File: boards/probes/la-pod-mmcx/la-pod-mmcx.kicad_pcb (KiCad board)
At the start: 4 copper layers, 80 x 20.8 mm, 16 parts, among them J1 MMCX-J-P-H-ST-EM1, J2 MMCX-J-P-H-ST-EM1, J3 MMCX-J-P-H-ST-EM1, J4 MMCX-J-P-H-ST-EM1, J5 LSHM-120-02.5-L-DV-A-N-K-TR, J6 MMCX-J-P-H-ST-EM1, J7 MMCX-J-P-H-ST-EM1, J8 MMCX-J-P-H-ST-EM1, J9 MMCX-J-P-H-ST-EM1, U1 24Cxx-DFN8

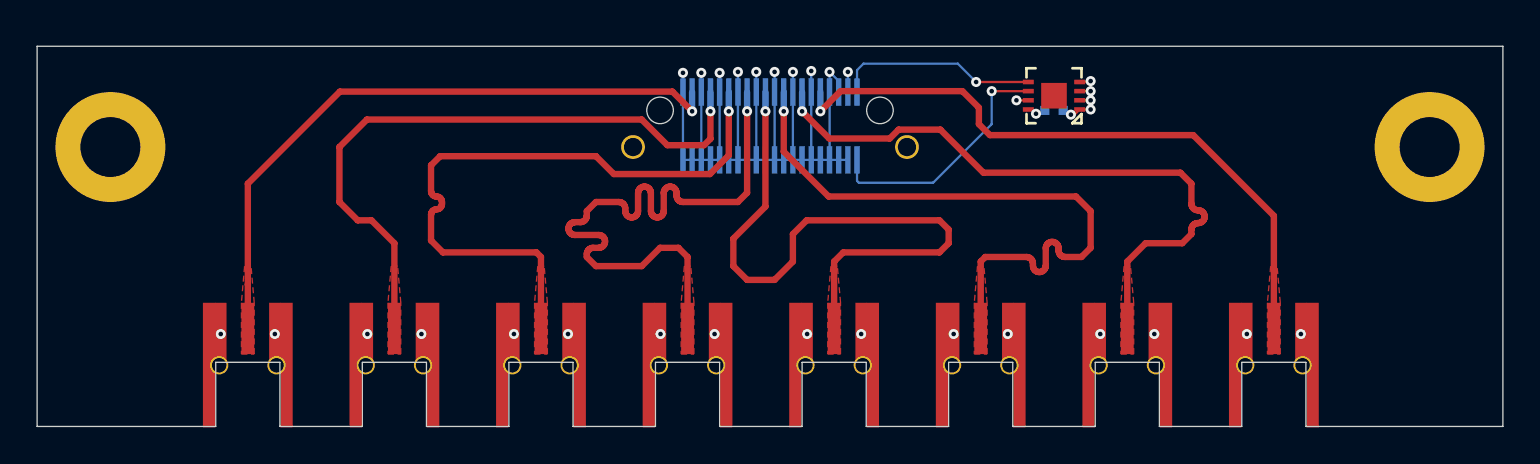
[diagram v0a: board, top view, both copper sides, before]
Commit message: Final version of la-pod-mmcx after layout review
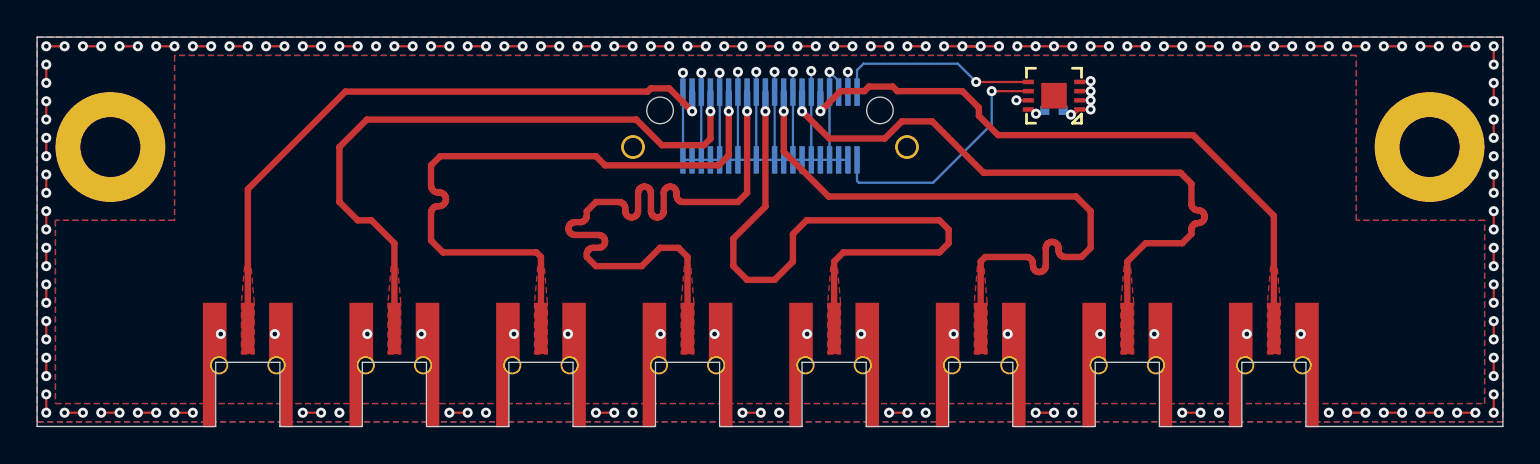
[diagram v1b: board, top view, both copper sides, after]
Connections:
- MH1 pad 1: (no net) -> /GND
- MH2 pad 1: (no net) -> /GND
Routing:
- net /GND: track 193.9 -> 393.0 mm, vias 30 -> 188
- added copper zone on B.Cu, net /GND
- added copper zone on F.Cu, net /GND
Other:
- board size 80 x 20.8 mm -> 80 x 21.2 mm
- board text added: "MEAD MMCX Input Bridge A. Zonenberg / v0.1 / 2020-06-03"
- board text removed: "MEAD MMCX Input Bridge A. Zonenberg / v0.1 / 2020-06-02"

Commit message: Tweaks to la-pod-mmcx mounting hole placement
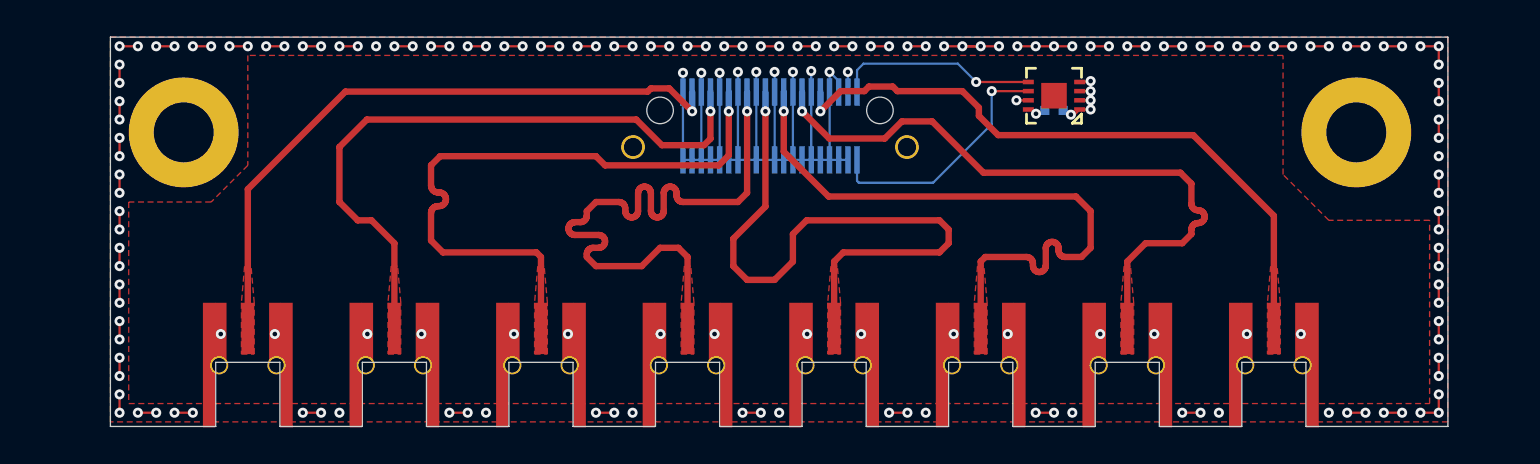
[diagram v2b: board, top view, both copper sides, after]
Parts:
- moved G*** 50.6 mm to (124.6, 56.9)
- moved MH1 4.08 mm to (70.5, 57.7)
- moved MH2 4.08 mm to (134.5, 57.7)
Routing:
- net /GND: track 393.0 -> 371.6 mm, vias 188 -> 174
- removed copper zone on B.Cu, net /GND
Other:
- board size 80 x 21.2 mm -> 73 x 21.2 mm

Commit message: la-pod-mmcx: fixed ground pours colliding with impedance matching cutouts, fixed missing soldermask cutouts on bottom side of board shield ring
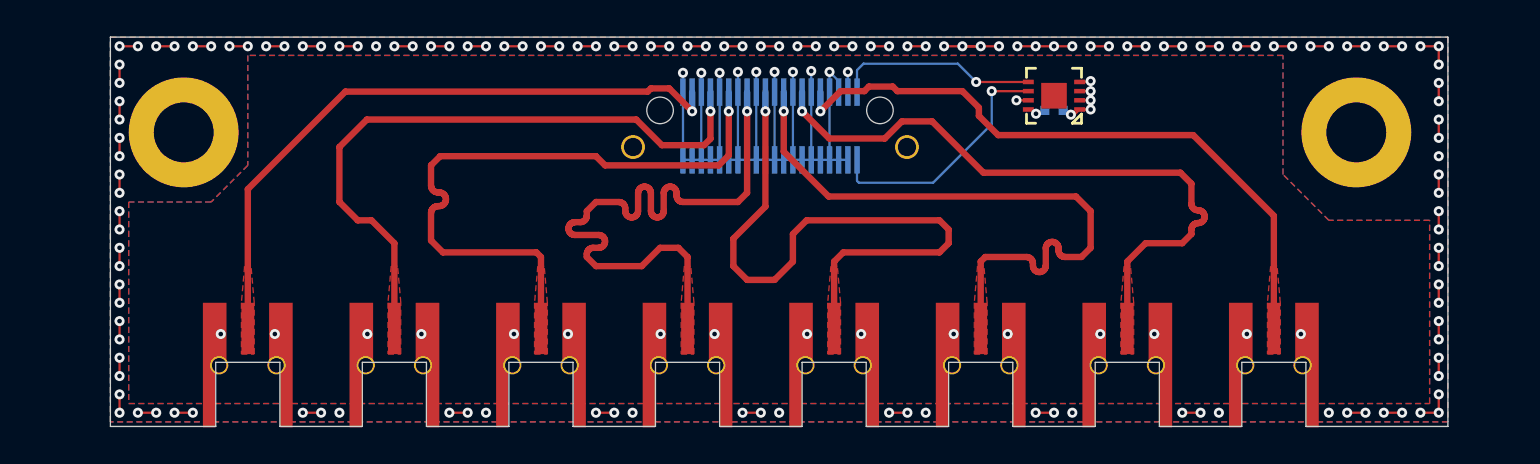
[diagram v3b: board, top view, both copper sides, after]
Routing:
- net /GND: track 371.6 -> 439.5 mm
- added copper zone on B.Cu, net /GND
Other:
- board text added: "MEAD MMCX Input Bridge A. Zonenberg / v0.1 / 2020-06-04"
- board text removed: "MEAD MMCX Input Bridge A. Zonenberg / v0.1 / 2020-06-03"
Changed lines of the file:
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@@
     (thickness 1.6)
     (drawings 37)
-    (tracks 801)
+    (tracks 822)
     (zones 0)
     (modules 16)
@@
     )
   )
-  (gr_text "MEAD MMCX Input Bridge\nA. Zonenberg / v0.1 / 2020-06-03" (at 82 63) (layer B.SilkS)
+  (gr_text "MEAD MMCX Input Bridge\nA. Zonenberg / v0.1 / 2020-06-04" (at 82 63) (layer B.SilkS)
     (effects (font (size 0.75 0.75) (thickness 0.1)) (justify mirror))
   )
@@
   (segment (start 123.475 68.705) (end 123.475 65.775) (width 0.125) (layer In1.Cu) (net 1))
   (segment (start 128.5 65.75) (end 123.5 65.75) (width 0.125) (layer In1.Cu) (net 1))
-  (segment (start 123.5 65.75) (end 120.75 65.75) (width 0.125) (layer In1.Cu) (net 1))
   (via (at 115.475 68.705) (size 0.55) (drill 0.25) (layers F.Cu B.Cu) (net 1))
   (via (at 112.525 68.705) (size 0.55) (drill 0.25) (layers F.Cu B.Cu) (net 1))
@@
   (segment (start 115.475 65.775) (end 115.5 65.75) (width 0.125) (layer In1.Cu) (net 1))
   (segment (start 115.475 68.705) (end 115.475 65.775) (width 0.125) (layer In1.Cu) (net 1))
-  (segment (start 115.5 65.75) (end 112.5 65.75) (width 0.125) (layer In1.Cu) (net 1))
   (via (at 107.475 68.705) (size 0.55) (drill 0.25) (layers F.Cu B.Cu) (net 1))
   (segment (start 107.475 65.775) (end 107.5 65.75) (width 0.125) (layer In1.Cu) (net 1))
-  (segment (start 112.5 65.75) (end 107.5 65.75) (width 0.125) (layer In1.Cu) (net 1))
   (segment (start 107.475 68.705) (end 107.475 65.775) (width 0.125) (layer In1.Cu) (net 1))
   (via (at 104.525 68.705) (size 0.55) (drill 0.25) (layers F.Cu B.Cu) (net 1))
   (segment (start 104.525 65.775) (end 104.5 65.75) (width 0.125) (layer In1.Cu) (net 1))
   (segment (start 104.525 68.705) (end 104.525 65.775) (width 0.125) (layer In1.Cu) (net 1))
-  (segment (start 107.5 65.75) (end 104.5 65.75) (width 0.125) (layer In1.Cu) (net 1))
   (via (at 99.475 68.705) (size 0.55) (drill 0.25) (layers F.Cu B.Cu) (net 1))
   (via (at 96.525 68.705) (size 0.55) (drill 0.25) (layers F.Cu B.Cu) (net 1))
@@
   (segment (start 104.5 65.75) (end 99.5 65.75) (width 0.125) (layer In1.Cu) (net 1))
   (segment (start 99.475 68.705) (end 99.475 65.775) (width 0.125) (layer In1.Cu) (net 1))
-  (segment (start 99.5 65.75) (end 96.5 65.75) (width 0.125) (layer In1.Cu) (net 1))
   (via (at 88.525 68.705) (size 0.55) (drill 0.25) (layers F.Cu B.Cu) (net 1))
   (via (at 91.475 68.705) (size 0.55) (drill 0.25) (layers F.Cu B.Cu) (net 1))
   (segment (start 91.475 65.775) (end 91.5 65.75) (width 0.125) (layer In1.Cu) (net 1))
   (segment (start 91.475 68.705) (end 91.475 65.775) (width 0.125) (layer In1.Cu) (net 1))
-  (segment (start 96.5 65.75) (end 91.5 65.75) (width 0.125) (layer In1.Cu) (net 1))
   (segment (start 88.5 67.2875) (end 88.5 65.75) (width 0.125) (layer In1.Cu) (net 1))
   (segment (start 88.525 67.3125) (end 88.5 67.2875) (width 0.125) (layer In1.Cu) (net 1))
   (segment (start 88.525 68.705) (end 88.525 67.3125) (width 0.125) (layer In1.Cu) (net 1))
-  (segment (start 91.5 65.75) (end 88.5 65.75) (width 0.125) (layer In1.Cu) (net 1))
   (via (at 83.475 68.705) (size 0.55) (drill 0.25) (layers F.Cu B.Cu) (net 1))
   (via (at 80.525 68.705) (size 0.55) (drill 0.25) (layers F.Cu B.Cu) (net 1))
@@
   (segment (start 83.475 68.705) (end 83.475 66.875) (width 0.125) (layer In1.Cu) (net 1))
   (segment (start 83.5 66.85) (end 83.5 65.75) (width 0.125) (layer In1.Cu) (net 1))
-  (segment (start 88.5 65.75) (end 83.5 65.75) (width 0.125) (layer In1.Cu) (net 1))
-  (segment (start 83.5 65.75) (end 80.5 65.75) (width 0.125) (layer In1.Cu) (net 1))
-  (via (at 75.475 68.705) (size 0.55) (drill 0.25) (layers F.Cu B.Cu) (net 1))
   (segment (start 75.475 68.705) (end 75.475 65.775) (width 0.125) (layer In1.Cu) (net 1))
   (segment (start 75.475 65.775) (end 75.5 65.75) (width 0.125) (layer In1.Cu) (net 1))
   (segment (start 80.5 65.75) (end 75.5 65.75) (width 0.125) (layer In1.Cu) (net 1))
-  (segment (start 131.475 66.875) (end 131.475 68.705) (width 0.125) (layer In1.Cu) (net 1))
-  (segment (start 130.35 65.75) (end 131.475 66.875) (width 0.125) (layer In1.Cu) (net 1))
-  (segment (start 128.5 65.75) (end 130.35 65.75) (width 0.125) (layer In1.Cu) (net 1))
   (segment (start 97.75 56.375) (end 97.75 59.2) (width 0.125) (layer B.Cu) (net 1))
   (segment (start 97.75 55.5) (end 97.75 56.375) (width 0.125) (layer B.Cu) (net 1))
@@
   (segment (start 99.75 65.5) (end 99.475 65.775) (width 0.125) (layer In1.Cu) (net 1))
   (segment (start 99.75 54.45) (end 99.75 65.5) (width 0.125) (layer In1.Cu) (net 1))
-  (via (at 72.525 68.705) (size 0.55) (drill 0.25) (layers F.Cu B.Cu) (net 1))
-  (segment (start 75.475 68.705) (end 72.525 68.705) (width 0.125) (layer In1.Cu) (net 1))
   (via (at 71 73) (size 0.55) (drill 0.25) (layers F.Cu B.Cu) (net 1))
   (segment (start 71 69.7925) (end 71 73) (width 0.125) (layer In1.Cu) (net 1))
@@
   (segment (start 139 54) (end 139 53) (width 0.125) (layer F.Cu) (net 1))
   (segment (start 139 72) (end 139 73) (width 0.125) (layer F.Cu) (net 1))
+  (segment (start 72.525 68.705) (end 72.525 63.175) (width 0.125) (layer In1.Cu) (net 1))
+  (segment (start 72.525 63.175) (end 73.25 62.45) (width 0.125) (layer In1.Cu) (net 1))
+  (segment (start 75.5 63.5) (end 75.5 65.75) (width 0.125) (layer In1.Cu) (net 1))
+  (segment (start 74.45 62.45) (end 75.5 63.5) (width 0.125) (layer In1.Cu) (net 1))
+  (via (at 72.525 68.705) (size 0.55) (drill 0.25) (layers F.Cu B.Cu) (net 1))
+  (via (at 75.475 68.705) (size 0.55) (drill 0.25) (layers F.Cu B.Cu) (net 1))
+  (segment (start 74.35 62.45) (end 74.45 62.45) (width 0.125) (layer In1.Cu) (net 1))
+  (segment (start 73.25 62.45) (end 74.35 62.45) (width 0.125) (layer In1.Cu) (net 1))
+  (segment (start 129.6 62.45) (end 131.475 64.325) (width 0.125) (layer In1.Cu) (net 1))
+  (segment (start 131.475 64.325) (end 131.475 67.125) (width 0.125) (layer In1.Cu) (net 1))
+  (segment (start 131.475 67.125) (end 131.475 68.705) (width 0.125) (layer In1.Cu) (net 1))
+  (segment (start 128.5 62.65) (end 128.3 62.45) (width 0.125) (layer In1.Cu) (net 1))
+  (segment (start 128.5 65.75) (end 128.5 62.65) (width 0.125) (layer In1.Cu) (net 1))
+  (segment (start 128.3 62.45) (end 129.6 62.45) (width 0.125) (layer In1.Cu) (net 1))
+  (segment (start 123.475 65.775) (end 123.475 62.475) (width 0.125) (layer In1.Cu) (net 1))
+  (segment (start 123.475 62.475) (end 123.45 62.45) (width 0.125) (layer In1.Cu) (net 1))
+  (segment (start 123.45 62.45) (end 128.3 62.45) (width 0.125) (layer In1.Cu) (net 1))
+  (segment (start 115.5 62.55) (end 115.6 62.45) (width 0.125) (layer In1.Cu) (net 1))
+  (segment (start 115.5 65.75) (end 115.5 62.55) (width 0.125) (layer In1.Cu) (net 1))
+  (segment (start 115.6 62.45) (end 123.45 62.45) (width 0.125) (layer In1.Cu) (net 1))
+  (segment (start 109.65 62.5) (end 109.7 62.45) (width 0.125) (layer In1.Cu) (net 1))
+  (segment (start 109.7 62.45) (end 115.6 62.45) (width 0.125) (layer In1.Cu) (net 1))
+  (segment (start 109.65 65.75) (end 107.5 65.75) (width 0.125) (layer In1.Cu) (net 1))
+  (segment (start 109.65 65.75) (end 109.65 62.5) (width 0.125) (layer In1.Cu) (net 1))
+  (segment (start 112.5 65.75) (end 109.65 65.75) (width 0.125) (layer In1.Cu) (net 1))
+  (segment (start 95.5 65.75) (end 95.5 62.45) (width 0.125) (layer In1.Cu) (net 1))
+  (segment (start 95.5 65.75) (end 91.5 65.75) (width 0.125) (layer In1.Cu) (net 1))
+  (segment (start 96.5 65.75) (end 95.5 65.75) (width 0.125) (layer In1.Cu) (net 1))
+  (segment (start 95.5 62.45) (end 95.4 62.45) (width 0.125) (layer In1.Cu) (net 1))
+  (segment (start 95.4 62.45) (end 109.7 62.45) (width 0.125) (layer In1.Cu) (net 1))
+  (segment (start 87.4 65.75) (end 87.4 62.55) (width 0.125) (layer In1.Cu) (net 1))
+  (segment (start 87.3 62.45) (end 95.4 62.45) (width 0.125) (layer In1.Cu) (net 1))
+  (segment (start 74.35 62.45) (end 87.3 62.45) (width 0.125) (layer In1.Cu) (net 1))
+  (segment (start 87.4 65.75) (end 83.5 65.75) (width 0.125) (layer In1.Cu) (net 1))
+  (segment (start 87.4 62.55) (end 87.3 62.45) (width 0.125) (layer In1.Cu) (net 1))
+  (segment (start 88.5 65.75) (end 87.4 65.75) (width 0.125) (layer In1.Cu) (net 1))
   (via (at 106.75 54.4) (size 0.55) (drill 0.25) (layers F.Cu B.Cu) (net 2))
   (segment (start 106.75 55.5) (end 106.75 54.4) (width 0.125) (layer B.Cu) (net 2))
@@
       )
     )
+  )
+  (zone (net 1) (net_name /GND) (layer B.Cu) (hatch edge 0.508)
+    (connect_pads yes (clearance 0.125))
+    (min_thickness 0.125)
+    (fill yes (arc_segments 32) (thermal_gap 0.125) (thermal_bridge_width 0.15))
+    (polygon
+      (pts
+        (xy 139.5 73.5) (xy 66.5 73.5) (xy 66.5 52.5) (xy 139.5 52.5)
+      )
+    )
+    (polygon
+      (pts
+        (xy 130.5 60) (xy 130.5 53.5) (xy 74 53.5) (xy 74 59.5) (xy 72 61.5)
+        (xy 67.5 61.5) (xy 67.5 72.5) (xy 138.5 72.5) (xy 138.5 62.5) (xy 133 62.5)
+      )
+    )
+  )
+  (zone (net 0) (net_name "") (layer B.Mask) (hatch edge 0.508)
+    (connect_pads yes (clearance 0.125))
+    (min_thickness 0.125)
+    (fill yes (arc_segments 32) (thermal_gap 0.125) (thermal_bridge_width 0.15))
+    (polygon
+      (pts
+        (xy 139.5 73.5) (xy 66.5 73.5) (xy 66.5 52.5) (xy 139.5 52.5)
+      )
+    )
+    (polygon
+      (pts
+        (xy 74 53.5) (xy 74 59.5) (xy 72 61.5) (xy 67.5 61.5) (xy 67.5 72.5)
+        (xy 138.5 72.5) (xy 138.5 62.5) (xy 133 62.5) (xy 130.5 60) (xy 130.5 53.5)
+      )
+    )
